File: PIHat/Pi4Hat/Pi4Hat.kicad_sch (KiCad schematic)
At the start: 14 parts, among them J1 GPIO, J2 U.FL-R-SMT-1_80_, J3 U.FL-R-SMT-1_80_, J4 U.FL-R-SMT-1_80_, J5 1725672, J6 1725672, J7 Conn_01x03_Socket, J8 GPIO

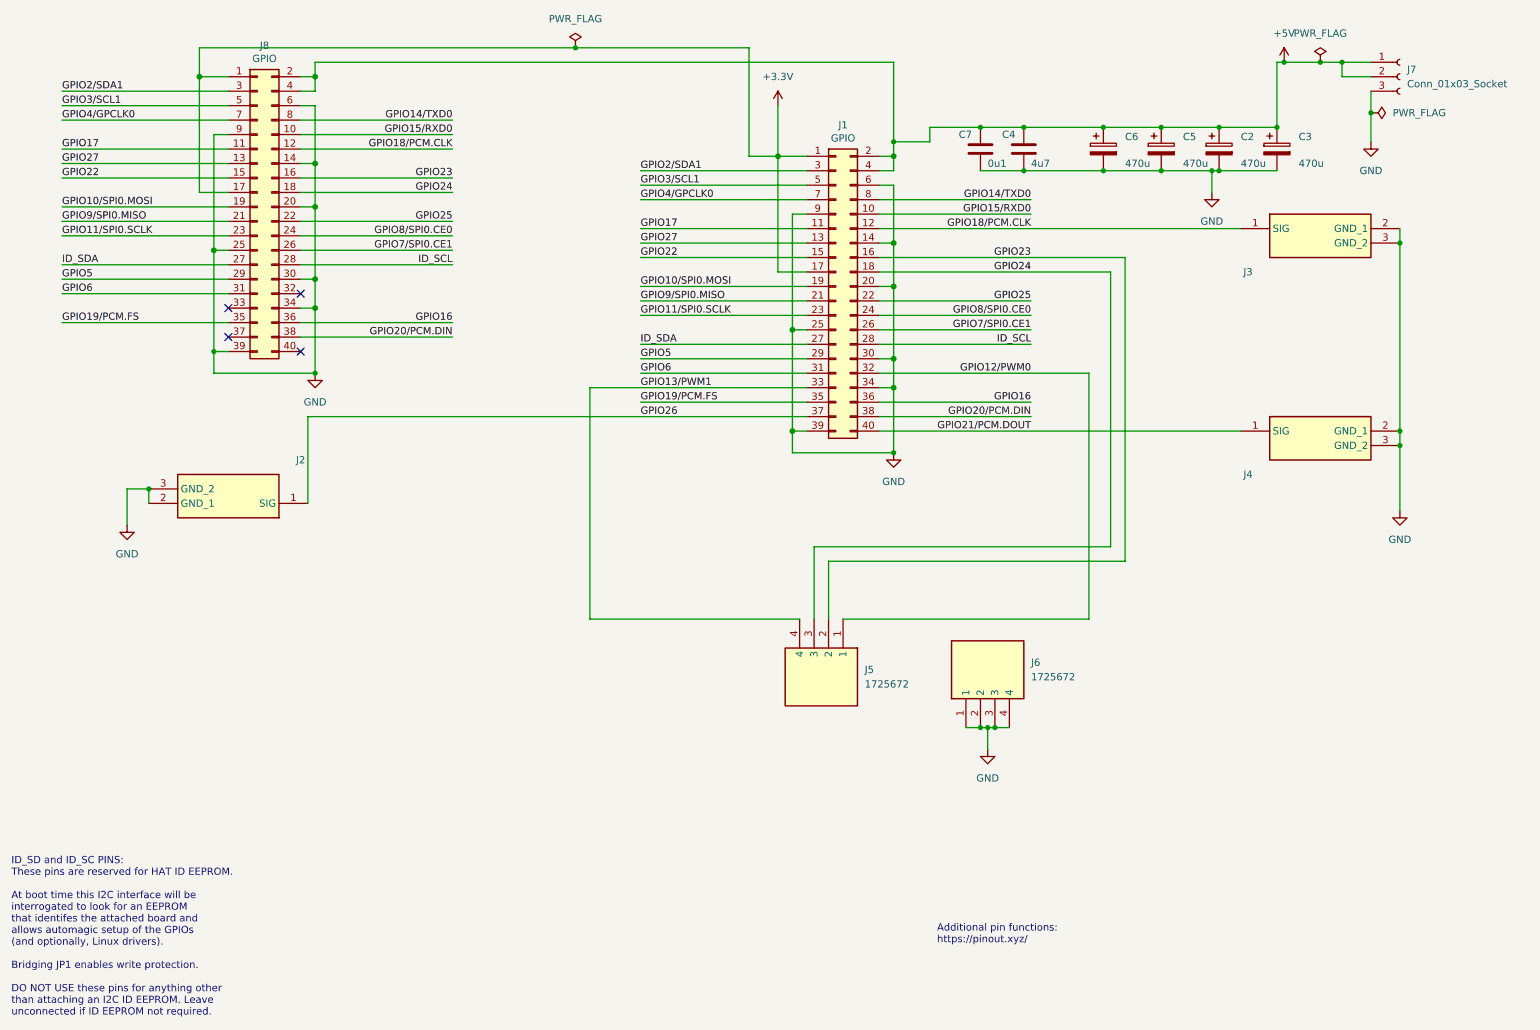
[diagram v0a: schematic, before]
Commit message: added new rpi power board
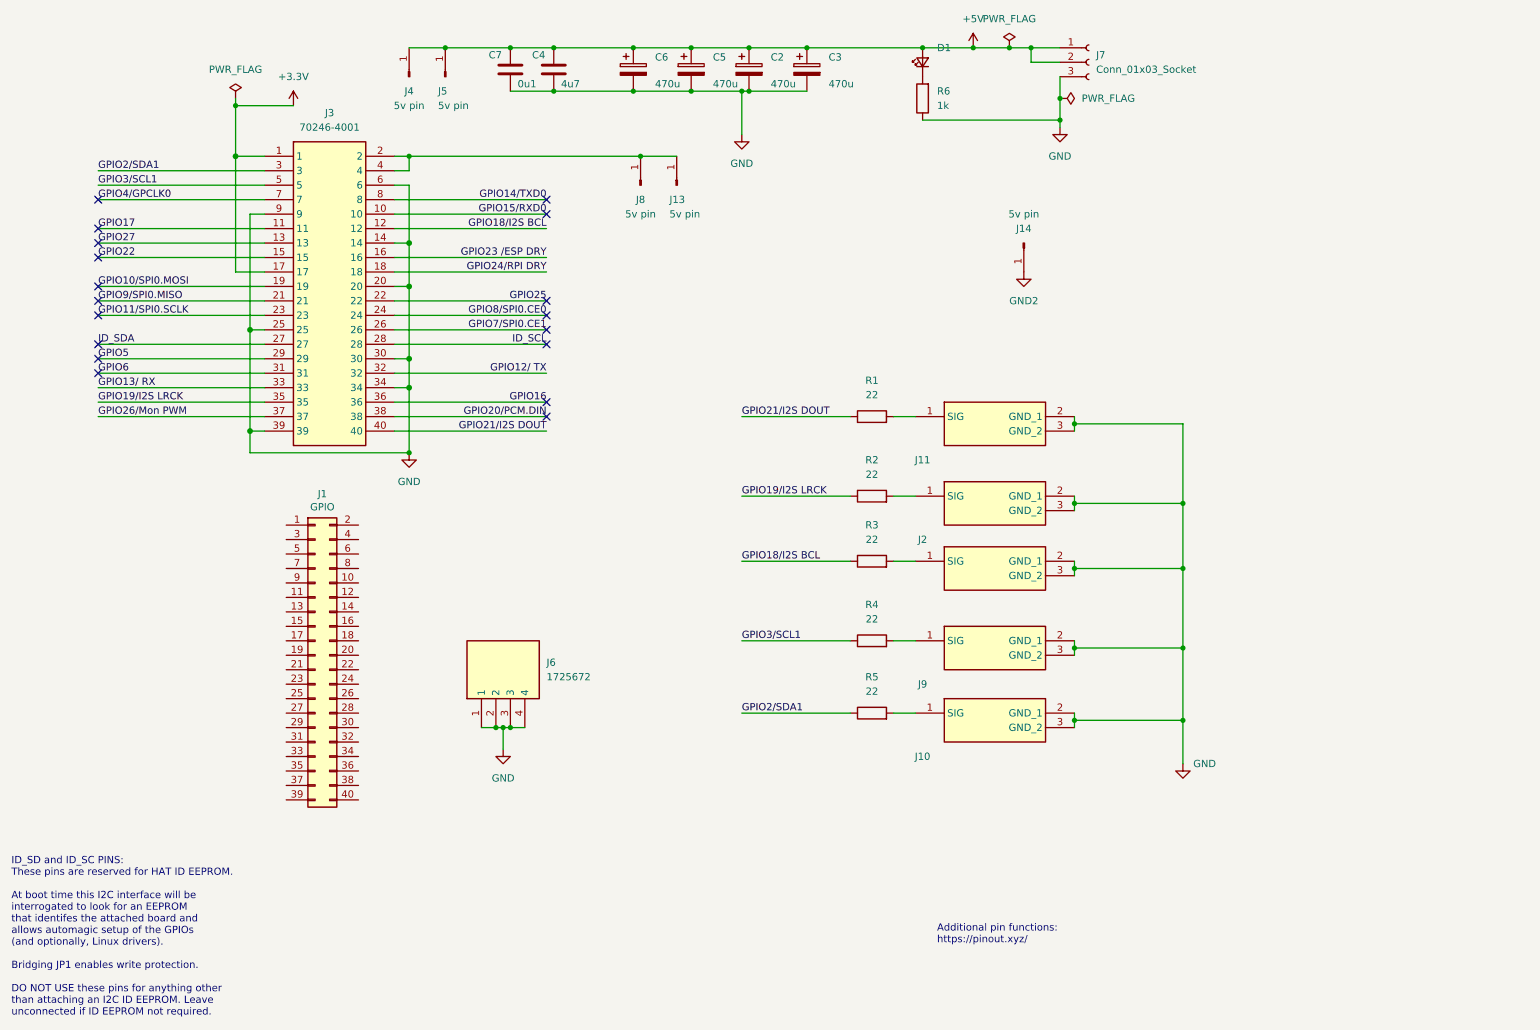
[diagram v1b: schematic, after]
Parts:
- removed J3, J4: U.FL-R-SMT-1_80_, UFLRSMT180, symbol NewSamsys:U.FL-R-SMT-1_80_
- removed J5: 1725672, 1725672, symbol NewSamsys:1725672
- removed J8: GPIO, Connector_PinSocket_2.54mm:PinSocket_2x20_P2.54mm_Vertical, symbol Connector_Generic:Conn_02x20_Odd_Even
- added D1: LS_R976, samsys:LEDC2012X40N, symbol Device:LED_Small
- added J10, J11, J12, J9: U.FL-R-SMT-1_80_, UFLRSMT180, symbol NewSamsys:U.FL-R-SMT-1_80_
- added J13, J14, J4, J5, J8: 5v pin, Connector_Pin:Pin_D0.7mm_L6.5mm_W1.8mm_FlatFork, symbol Connector:Conn_01x01_Pin
- added J3: 70246-4001, samsys:SHDR40W64P254_2X20_5842X889X947P, symbol NewSamsys:70246-4001
- added R1, R2, R3, R4, R5: 22, Resistor_SMD:R_0402_1005Metric, symbol Device:R
- added R6: 1k, Resistor_SMD:R_0402_1005Metric, symbol Device:R
- C2, C3, C5, C6: footprint Capacitor_THT:CP_Radial_D13.0mm_P5.00mm -> Capacitor_THT:CP_Radial_D10.0mm_P5.00mm
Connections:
- net +3.3V: now also J3.1, J3.17; no longer J1.1 (Pin_1), J1.17 (Pin_17)
- net +5V: now also D1.2 (A), J4.1 (Pin_1), J5.1 (Pin_1); no longer J1.2 (Pin_2), J1.4 (Pin_4)
- net GND: now also J10.2 (GND_1), J10.3 (GND_2), J11.2 (GND_1), J11.3 (GND_2), J12.2 (GND_1), J12.3 (GND_2), J3.14, J3.20, J3.25, J3.30, J3.34, J3.39, J3.6, J3.9, J9.2 (GND_1), J9.3 (GND_2), R6.1; no longer J1.14 (Pin_14), J1.20 (Pin_20), J1.25 (Pin_25), J1.30 (Pin_30), J1.34 (Pin_34), J1.39 (Pin_39), J1.6 (Pin_6), J1.9 (Pin_9)
- net GPIO10/SPI0.MOSI: now also J3.19; no longer J1.19 (Pin_19)
- net GPIO11/SPI0.SCLK: now also J3.23; no longer J1.23 (Pin_23)
- net GPIO14/TXD0: now also J3.8; no longer J1.8 (Pin_8)
- net GPIO15/RXD0: now also J3.10; no longer J1.10 (Pin_10)
- net GPIO16: now also J3.36; no longer J1.36 (Pin_36)
- net GPIO17: now also J3.11; no longer J1.11 (Pin_11)
- net GPIO20/PCM.DIN: now also J3.38; no longer J1.38 (Pin_38)
- net GPIO22: now also J3.15; no longer J1.15 (Pin_15)
- net GPIO25: now also J3.22; no longer J1.22 (Pin_22)
- net GPIO27: now also J3.13; no longer J1.13 (Pin_13)
- net GPIO2/SDA1: now also J3.3, R5.1; no longer J1.3 (Pin_3)
- net GPIO3/SCL1: now also J3.5, R4.1; no longer J1.5 (Pin_5)
- net GPIO4/GPCLK0: now also J3.7; no longer J1.7 (Pin_7)
- net GPIO5: now also J3.29; no longer J1.29 (Pin_29)
- net GPIO6: now also J3.31; no longer J1.31 (Pin_31)
- net GPIO7/SPI0.CE1: now also J3.26; no longer J1.26 (Pin_26)
- net GPIO8/SPI0.CE0: now also J3.24; no longer J1.24 (Pin_24)
- net GPIO9/SPI0.MISO: now also J3.21; no longer J1.21 (Pin_21)
- net ID_SCL: now also J3.28; no longer J1.28 (Pin_28)
- net ID_SDA: now also J3.27; no longer J1.27 (Pin_27)
- net GPIO12/PWM0: no longer names the net of J1.32 (Pin_32)
- net GPIO13/PWM1: no longer names the net of J1.33 (Pin_33)
- net GPIO18/PCM.CLK: no longer names the net of J1.12 (Pin_12)
- net GPIO19/PCM.FS: no longer names the net of J1.35 (Pin_35)
- net GPIO21/PCM.DOUT: no longer names the net of J1.40 (Pin_40)
- net GPIO23: no longer names the net of J1.16 (Pin_16)
- net GPIO24: no longer names the net of J1.18 (Pin_18)
- net GPIO26: no longer names the net of J2.1 (SIG)
- net GPIO26: now also R2.2; no longer J1.37 (Pin_37)
- new net: J13.1 (Pin_1), J3.2, J3.4, J8.1 (Pin_1)
- new net: J12.1 (SIG), R3.2
- new net: D1.1 (K), R6.2
- new net: J10.1 (SIG), R5.2
- new net: J11.1 (SIG), R1.2
- new net: J9.1 (SIG), R4.2
- new net GND2: J14.1 (Pin_1)
- new net GPIO12/ TX: J3.32
- new net GPIO13/ RX: J3.33
- new net GPIO18/I2S BCL: J3.12, R3.1
- new net GPIO19/I2S LRCK: J3.35, R2.1
- new net GPIO21/I2S DOUT: J3.40, R1.1
- new net GPIO23 /ESP DRY: J3.16
- new net GPIO24/RPI DRY: J3.18
- new net GPIO26/Mon PWM: J3.37
- no-connect marks 4 -> 18
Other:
- moved on the sheet: C2, C3, C4, C5, C6, C7, J2, J6, J7
